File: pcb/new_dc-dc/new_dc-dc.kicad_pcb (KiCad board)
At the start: 2 copper layers, 22 parts, among them J1 power, U1 LMR16030SDDAR

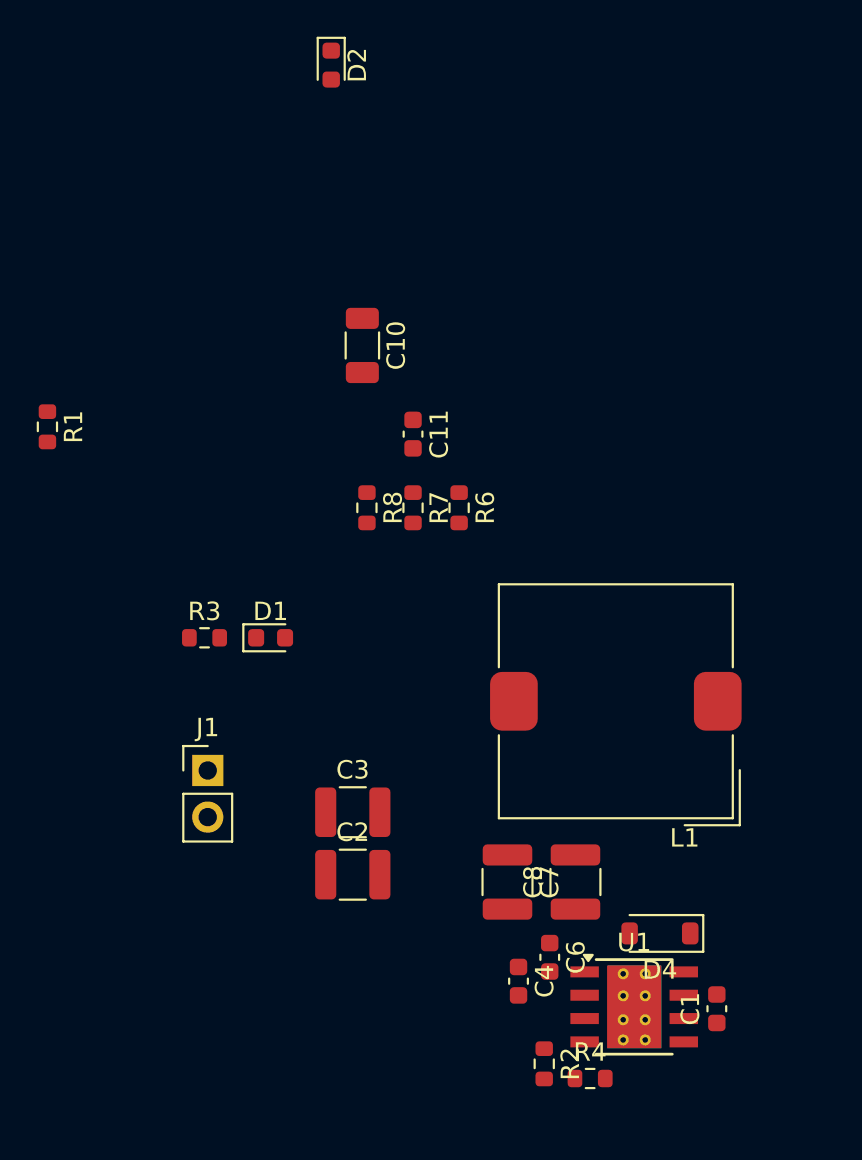
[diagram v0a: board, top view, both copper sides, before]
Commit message: feat: new_dc-dc pcb
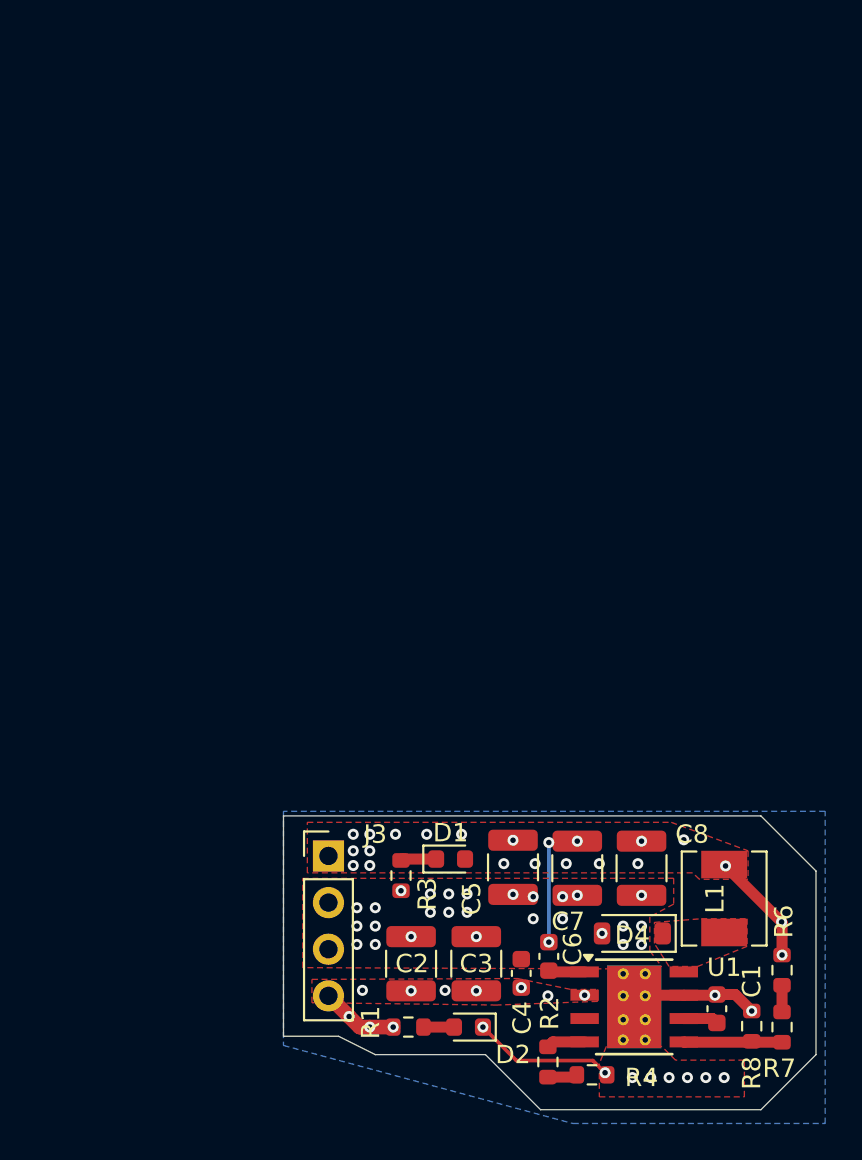
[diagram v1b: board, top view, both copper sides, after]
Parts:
- removed C10: 4.7uf/50v, Capacitor_SMD:C_1206_3216Metric
- removed C11: 100nf/50v, Capacitor_SMD:C_0603_1608Metric
- removed J1: power, Connector_PinHeader_2.54mm:PinHeader_1x02_P2.54mm_Vertical
- added C5: 10uF/35v, Capacitor_SMD:C_1210_3225Metric, F.Cu at (150.5, 103.8)
- added J3: Conn_01x04_Pin, Connector_PinHeader_2.54mm:PinHeader_1x04_P2.54mm_Vertical, F.Cu at (140.4, 103.2)
- L1: value 22uH -> 6.8uH; footprint Inductor_SMD:L_TDK_SLF12565 -> Inductor_SMD:L_Chilisin_BMRA00040420
- moved D2 52.9 mm to (148.1, 112.5), turned to 180 degrees
- moved R1 38.1 mm to (144.8, 112.5), turned to 0 degrees
- moved R8 35.2 mm to (163.5, 112.5), turned to 90 degrees
- moved R7 34.7 mm to (165.2, 112.5)
- moved R6 30.7 mm to (165.2, 109.4)
- moved R3 16.8 mm to (144.4, 104.2), turned to -90 degrees
- moved D1 15.5 mm to (147.1, 103.3)
- moved L1 12.3 mm to (162.0, 105.5), turned to 90 degrees
- moved C3 10.6 mm to (148.5, 109.0), turned to 90 degrees
- moved C2 5.80 mm to (144.9, 109.0), turned to 90 degrees
- moved C7 3.87 mm to (154.0, 103.8)
- moved C8 3.68 mm to (157.5, 103.8)
- moved D4 1.50 mm to (157.0, 107.4)
- moved C4 0.45 mm to (150.9, 109.6)
- moved R2 0.22 mm to (152.4, 114.4)
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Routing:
- net GND: track 0.00 -> 14.0 mm, vias 0 -> 37
- net 24V/3A: track 0.00 -> 11.7 mm, vias 0 -> 23
- net Net-(U1-FB): track 0.00 -> 5.36 mm
- net VCC: track 0.00 -> 4.23 mm, vias 0 -> 10
- net Net-(U1-RT/YNC): track 0.00 -> 2.11 mm
- net Net-(U1-BOOT): track 0.00 -> 1.98 mm
- net Net-(D1-K): track 0.00 -> 1.94 mm
- net Net-(U1-SS/PGOOD): track 0.00 -> 1.90 mm
- net Net-(D2-A): track 0.00 -> 1.66 mm
- net Net-(R2-Pad2): track 0.00 -> 1.63 mm
- net Net-(R6-Pad2): track 0.00 -> 1.45 mm
- added copper zone on F.Cu, net 24V/3A
- added copper zone on In2.Cu, net 24V/3A
- added copper zone on In4.Cu, net 24V/3A
- added copper zone on B.Cu, net GND
- added copper zone on F.Cu, net GND
- added copper zone on F.Cu, net Net-(D4-K)
- added copper zone on F.Cu, net VCC
- added copper zone on In1.Cu, net VCC
- added copper zone on In3.Cu, net VCC
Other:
- board outline added: 29 x 16 mm
- copper layers 2 -> 6
